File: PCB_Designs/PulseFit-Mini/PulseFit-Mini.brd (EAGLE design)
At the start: 25.4 x 25.4 mm, 28 parts

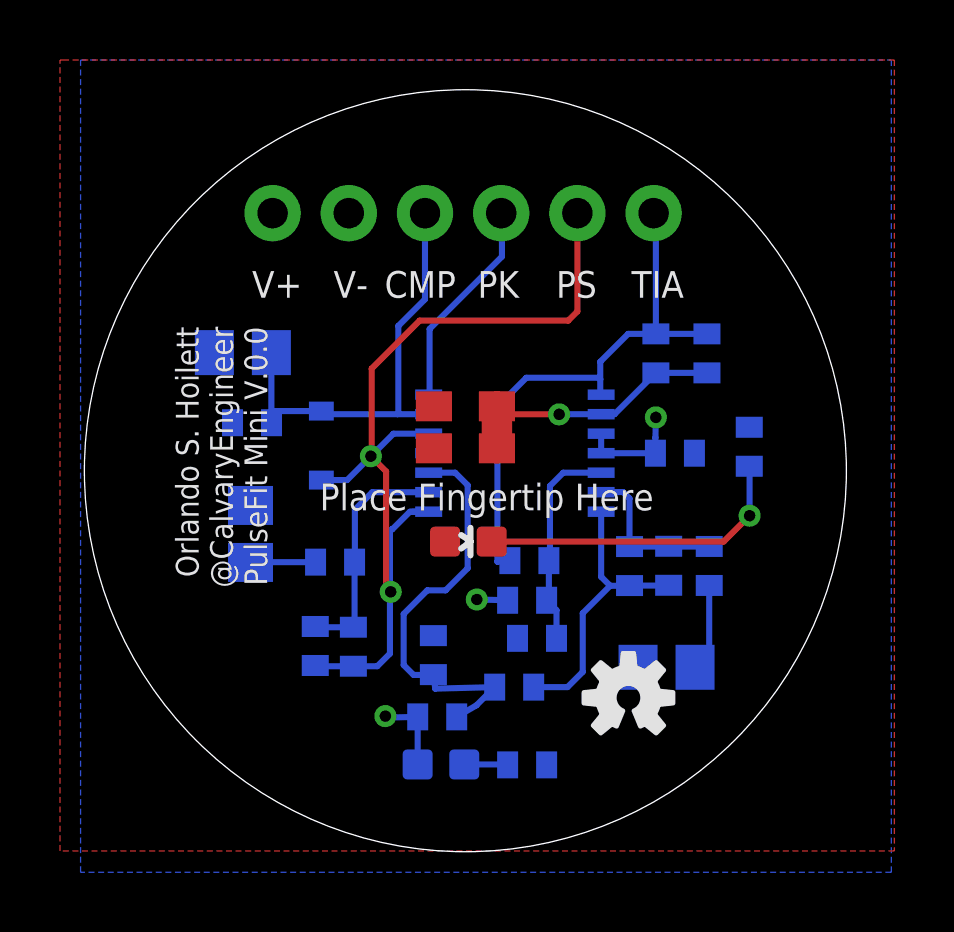
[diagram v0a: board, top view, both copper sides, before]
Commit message: updated BOM for PulseFit Mini
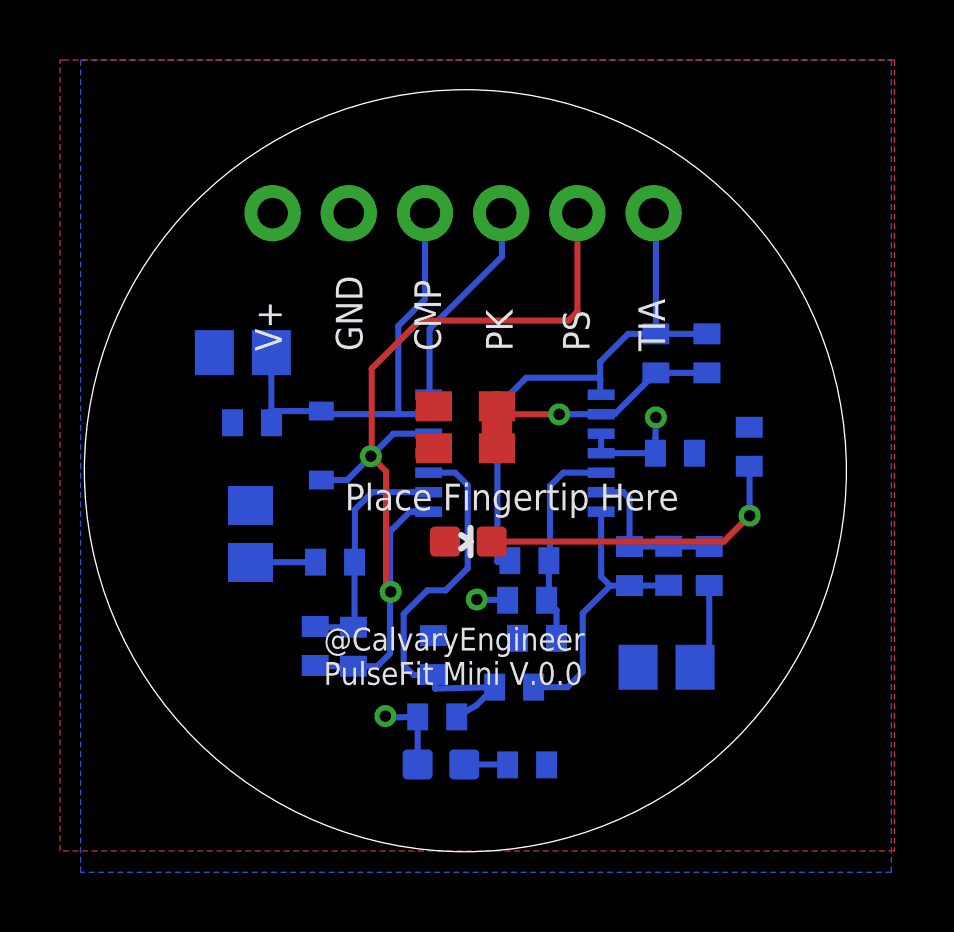
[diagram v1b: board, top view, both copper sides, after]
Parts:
- moved LOGO1 13.5 mm to (6.30, 6.30), flipped to the bottom
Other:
- board text added: "@CalvaryEngineer PulseFit Mini V.0.0"
- board text added: "GND"
- board text removed: "Orlando S. Hoilett @CalvaryEngineer PulseFit Mini V.0.0"
- board text removed: "V-"
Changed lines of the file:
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@@
 <board>
 <plain>
-<text x="11.5316" y="18.034" size="0.889" layer="25">CMP</text>
-<text x="14.6304" y="18.034" size="0.889" layer="25">PK</text>
-<text x="17.2466" y="18.034" size="0.889" layer="25">PS</text>
-<text x="7.112" y="18.034" size="0.889" layer="25">V+</text>
-<text x="9.8298" y="18.034" size="0.889" layer="25">V-</text>
-<text x="4.572" y="17.0688" size="0.762" layer="25" rot="R270">Orlando S. Hoilett
-@CalvaryEngineer
+<text x="13.4112" y="16.256" size="0.889" layer="25" rot="R90">CMP</text>
+<text x="15.7988" y="16.256" size="0.889" layer="25" rot="R90">PK</text>
+<text x="18.3642" y="16.256" size="0.889" layer="25" rot="R90">PS</text>
+<text x="8.1026" y="16.256" size="0.889" layer="25" rot="R90">V+</text>
+<text x="10.795" y="16.256" size="0.889" layer="25" rot="R90">GND</text>
+<text x="9.4996" y="5.1308" size="0.762" layer="25">@CalvaryEngineer
 PulseFit Mini V.0.0</text>
 <text x="11.7602" y="2.8194" size="0.762" layer="26" rot="R180">PWR</text>
-<text x="20.4978" y="11.8364" size="0.889" layer="121" rot="R180">Place Fingertip Here</text>
+<text x="21.336" y="11.8364" size="0.889" layer="121" rot="R180">Place Fingertip Here</text>
 <text x="-0.889" y="25.1714" size="0.889" layer="108">Creative Commons License
 Attribution-NonCommercial-
 ShareAlike 4.0 Unported </text>
 <circle x="14.224" y="12.2682" radius="12.7" width="0.002540625" layer="20"/>
-<text x="19.7612" y="18.034" size="0.889" layer="25">TIA</text>
+<text x="20.8788" y="16.256" size="0.889" layer="25" rot="R90">TIA</text>
 <text x="30.4292" y="26.3144" size="0.635" layer="108" rot="R180">NOTE: This is NOT a medical device</text>
 <dimension x1="14.20304375" y1="24.96818125" x2="14.24495625" y2="-0.43178125" x3="29.6164" y3="12.293596875" textsize="1.016" layer="108" dtype="diameter"/>
@@
 </element>
 <element name="C5" library="resistor" package="C0402" value="10n" x="9.2202" y="6.4262" smashed="yes" rot="MR270">
-<attribute name="NAME" x="8.509" y="5.08" size="0.762" layer="26" rot="MR180"/>
+<attribute name="NAME" x="8.509" y="4.8514" size="0.762" layer="26" rot="MR180"/>
 <attribute name="VALUE" x="11.1252" y="7.0612" size="1.27" layer="28" rot="MR270"/>
 </element>
 <element name="C6" library="resistor" package="C0805" value="10u" x="6.8072" y="16.2052" smashed="yes" rot="MR180">
-<attribute name="NAME" x="3.8354" y="15.5194" size="0.762" layer="26" rot="MR90"/>
+<attribute name="NAME" x="7.0358" y="17.7038" size="0.762" layer="26" rot="MR0"/>
 <attribute name="VALUE" x="6.1722" y="18.1102" size="1.27" layer="28" rot="MR180"/>
 </element>
@@
 <element name="D1" library="SparkFun-DiscreteSemi" package="SOD-323" value="250mA/100V" x="9.4234" y="13.1064" smashed="yes" rot="MR270">
 <attribute name="PROD_ID" value="DIO-09646" x="9.4234" y="13.1064" size="1.778" layer="28" rot="MR270" display="off"/>
-<attribute name="NAME" x="9.1948" y="15.8242" size="0.762" layer="26" rot="MR180"/>
+<attribute name="NAME" x="9.271" y="15.9766" size="0.762" layer="26" rot="MR180"/>
 <attribute name="VALUE" x="10.8204" y="14.1224" size="0.4064" layer="28" rot="MR270"/>
 </element>
@@
 </element>
 <element name="R10" library="resistor" package="R0402" value="3.3M" x="10.4902" y="6.4008" smashed="yes" rot="MR270">
-<attribute name="NAME" x="11.3538" y="5.715" size="0.762" layer="26" rot="MR90"/>
+<attribute name="NAME" x="11.4554" y="5.3086" size="0.762" layer="26" rot="MR90"/>
 <attribute name="VALUE" x="12.3952" y="7.0358" size="1.27" layer="28" rot="MR270"/>
 </element>
 <element name="R11" library="resistor" package="R0402" value="32k" x="9.8806" y="9.2202" smashed="yes" rot="MR180">
-<attribute name="NAME" x="10.5918" y="10.2108" size="0.762" layer="26" rot="MR0"/>
+<attribute name="NAME" x="10.5664" y="10.1854" size="0.762" layer="26" rot="MR0"/>
 <attribute name="VALUE" x="9.2456" y="11.1252" size="1.27" layer="28" rot="MR180"/>
 </element>
 <element name="R12" library="resistor" package="R0402" value="1.5M" x="7.112" y="13.8684" smashed="yes" rot="MR0">
-<attribute name="NAME" x="3.7338" y="14.097" size="0.762" layer="26" rot="MR180"/>
+<attribute name="NAME" x="4.699" y="12.3952" size="0.762" layer="26" rot="MR90"/>
 <attribute name="VALUE" x="7.747" y="11.9634" size="1.27" layer="28" rot="MR0"/>
 </element>
 <element name="R8" library="resistor" package="R0402" value="1.5M" x="13.2842" y="4.064" smashed="yes" rot="MR180">
-<attribute name="NAME" x="14.732" y="4.2672" size="0.762" layer="26" rot="MR180"/>
+<attribute name="NAME" x="14.8082" y="4.1402" size="0.762" layer="26" rot="MR180"/>
 <attribute name="VALUE" x="12.6492" y="5.969" size="1.27" layer="28" rot="MR180"/>
 </element>
 <element name="R9" library="resistor" package="R0402" value="1.5M" x="13.1572" y="6.1214" smashed="yes" rot="MR90">
-<attribute name="NAME" x="12.7" y="8.2804" size="0.762" layer="26" rot="MR180"/>
+<attribute name="NAME" x="12.5984" y="8.2804" size="0.762" layer="26" rot="MR180"/>
 <attribute name="VALUE" x="11.2522" y="5.4864" size="1.27" layer="28" rot="MR90"/>
 </element>
@@
 </element>
 <element name="R15" library="resistor" package="R0402" value="1k" x="16.2814" y="2.4638" smashed="yes" rot="MR180">
-<attribute name="NAME" x="18.4912" y="3.9624" size="0.762" layer="26" rot="MR270"/>
+<attribute name="NAME" x="18.6182" y="3.5814" size="0.762" layer="26" rot="MR270"/>
 <attribute name="VALUE" x="15.6464" y="4.3688" size="1.27" layer="28" rot="MR180"/>
 </element>
@@
 </element>
 <element name="C11" library="resistor" package="C0402" value="10n" x="21.0002" y="9.0984" smashed="yes" rot="MR270">
-<attribute name="NAME" x="20.2386" y="11.3228" size="0.762" layer="26" rot="MR180"/>
+<attribute name="NAME" x="20.2132" y="11.3228" size="0.762" layer="26" rot="MR180"/>
 <attribute name="VALUE" x="22.9052" y="9.7334" size="1.27" layer="28" rot="MR270"/>
 </element>
 <element name="LED13" library="SparkFun-LED" package="LED-0603" value="" x="13.3094" y="2.4768" smashed="yes" rot="MR90"/>
-<element name="LOGO1" library="SparkFun-Aesthetics" package="OSHW-LOGO-S" value="OSHW-LOGOS" x="19.6596" y="4.699" smashed="yes"/>
+<element name="LOGO1" library="SparkFun-Aesthetics" package="OSHW-LOGO-S" value="OSHW-LOGOS" x="6.2992" y="6.2992" smashed="yes" rot="MR0"/>
 <element name="C3" library="resistor" package="C0805" value="10u" x="7.0612" y="10.16" smashed="yes" rot="MR270">
 <attribute name="NAME" x="5.6388" y="10.7696" size="0.762" layer="26" rot="MR270"/>
@@
 </element>
 <element name="C2" library="resistor" package="C0402" value="470n" x="16.3576" y="9.271" smashed="yes" rot="MR180">
-<attribute name="NAME" x="14.2494" y="8.6868" size="0.762" layer="26" rot="MR90"/>
+<attribute name="NAME" x="14.097" y="8.5598" size="0.762" layer="26" rot="MR90"/>
 <attribute name="VALUE" x="15.7226" y="11.176" size="1.27" layer="28" rot="MR180"/>
 </element>
 <element name="R3" library="resistor" package="R0402" value="1.5M" x="16.2814" y="7.9502" smashed="yes" rot="MR180">
-<attribute name="NAME" x="17.7292" y="7.4422" size="0.762" layer="26" rot="MR90"/>
+<attribute name="NAME" x="17.7292" y="7.5438" size="0.762" layer="26" rot="MR90"/>
 <attribute name="VALUE" x="15.6464" y="9.8552" size="1.27" layer="28" rot="MR180"/>
 </element>
@@
 </element>
 <element name="R5" library="resistor" package="R0402" value="32k" x="22.352" y="9.0932" smashed="yes" rot="MR90">
-<attribute name="NAME" x="23.241" y="8.1026" size="0.762" layer="26" rot="MR90"/>
+<attribute name="NAME" x="23.3172" y="8.3058" size="0.762" layer="26" rot="MR90"/>
 <attribute name="VALUE" x="20.447" y="8.4582" size="1.27" layer="28" rot="MR90"/>
 </element>
 <element name="C8" library="resistor" package="C0805" value="10u" x="20.9296" y="5.715" smashed="yes" rot="MR180">
-<attribute name="NAME" x="19.9136" y="4.5212" size="0.762" layer="26" rot="MR180"/>
+<attribute name="NAME" x="19.7866" y="4.3434" size="0.762" layer="26" rot="MR180"/>
 <attribute name="VALUE" x="19.6596" y="8.255" size="1.27" layer="28" rot="MR180"/>
 </element>
